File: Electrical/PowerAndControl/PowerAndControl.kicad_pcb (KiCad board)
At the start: 2 copper layers, 65 x 30 mm, 21 parts, among them J1 Conn_02x03_Counter_Clockwise, SW2 SW_SPDT_312, U1 MCP73811T-420I-OT, U2 TPS22919QDCKRQ1, U3 TPS3840PL30DBVR

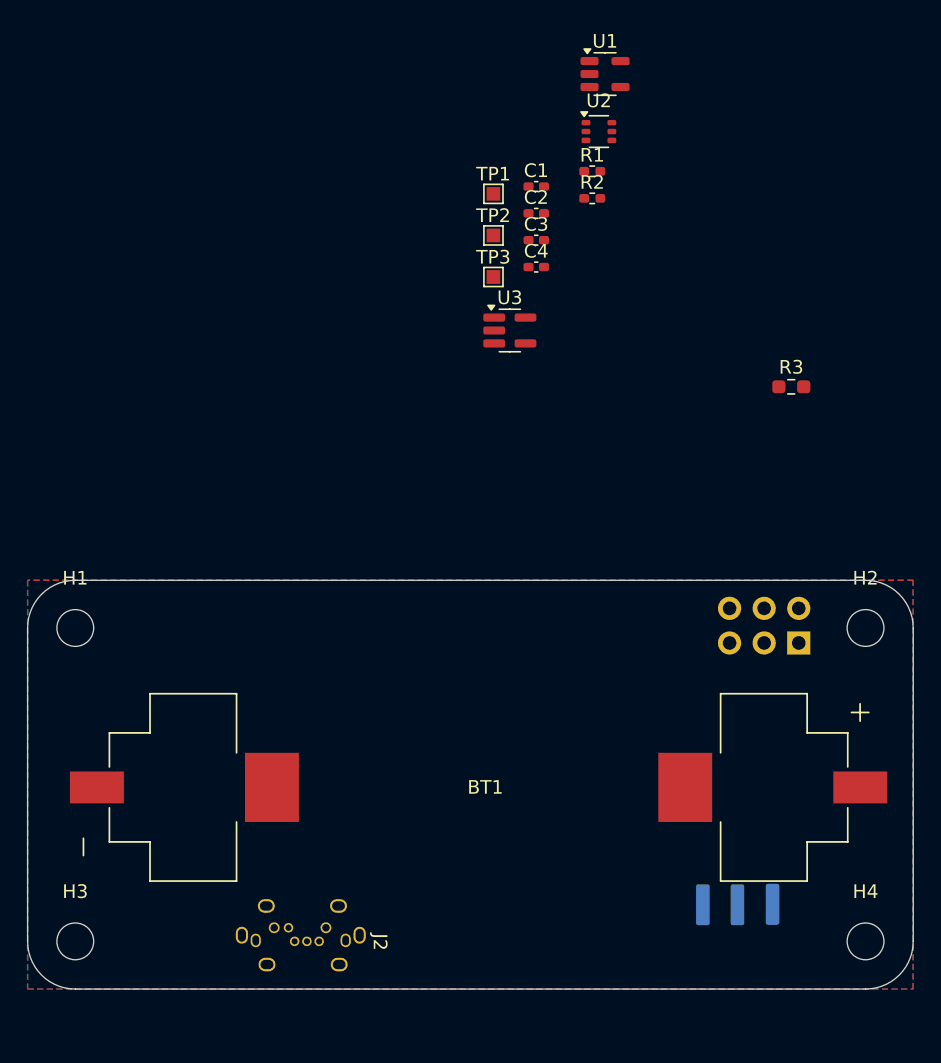
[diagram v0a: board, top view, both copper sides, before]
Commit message: Layout of AA variant complete.  Need to check pinout 2x more
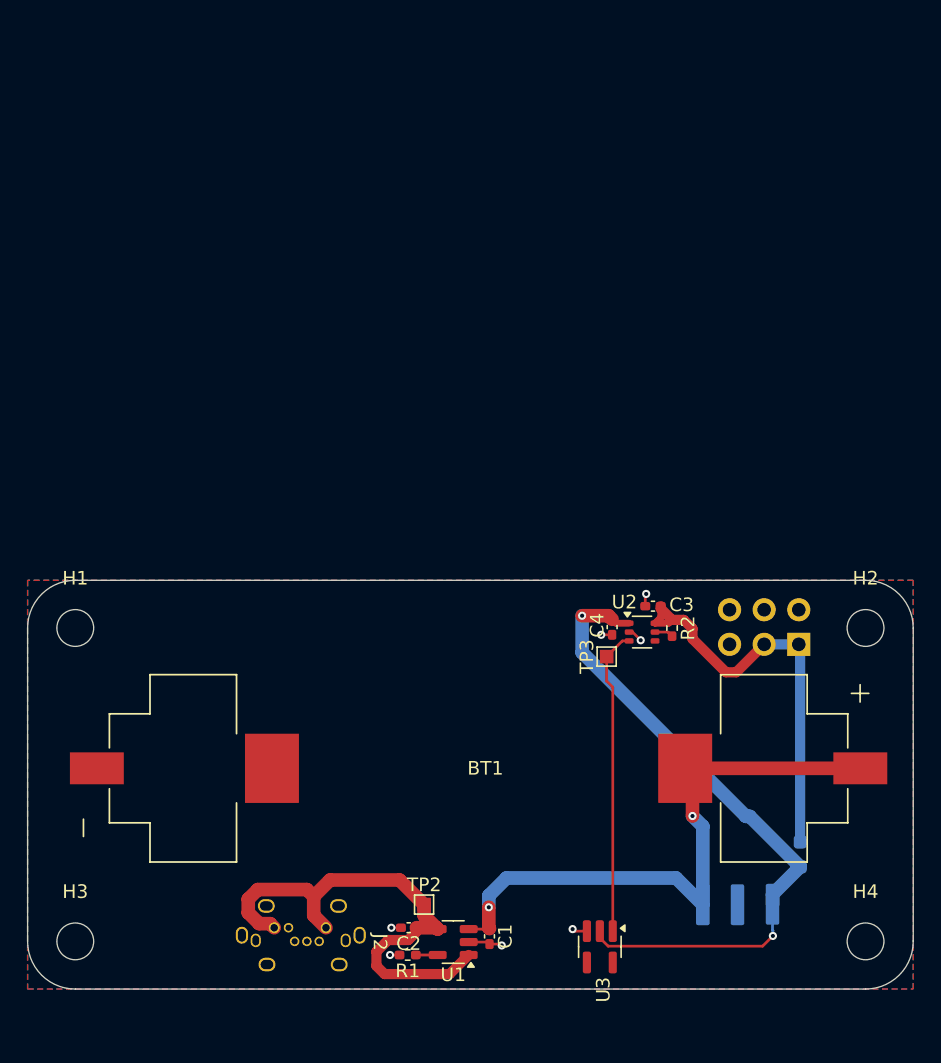
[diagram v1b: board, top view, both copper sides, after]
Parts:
- removed TP1: TestPoint, TestPoint:TestPoint_Pad_1.0x1.0mm
- R3: moved to B.Cu
- moved U1 64.7 mm to (127.7, 123.0), turned to 180 degrees
- moved R1 59.1 mm to (124.4, 124.0), turned to 180 degrees
- moved C1 55.1 mm to (130.4, 122.6), turned to -90 degrees
- moved C2 53.3 mm to (124.5, 122.0), turned to 180 degrees
- moved TP2 49.4 mm to (125.6, 120.3)
- moved U3 45.7 mm to (138.5, 123.4), turned to -90 degrees
- moved U2 36.9 mm to (141.6, 100.3)
- moved R3 34.3 mm to (153.2, 116.6), turned to 90 degrees
- moved R2 32.1 mm to (143.8, 100.0), turned to -90 degrees
- moved TP3 29.1 mm to (139.0, 102.1), turned to 90 degrees
- moved C3 28.2 mm to (142.4, 98.4), turned to 180 degrees
- moved C4 27.0 mm to (139.4, 99.9), turned to -90 degrees
- moved BT1 1.40 mm to (129.6, 110.3)
- moved J1 0.10 mm to (153.1, 101.2)
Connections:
- J1 pad 1: unconnected-(J1-Pin_1-Pad1) -> /VBAT_OUT
- J1 pad 3: unconnected-(J1-Pin_3-Pad3) -> /VBAT_OUT
- J1 pad 4: GND -> unconnected-(J1-Pin_4-Pad4)
- J1 pad 5: /VBAT_OUT -> GND
- J1 pad 6: /VBAT_OUT -> unconnected-(J1-Pin_6-Pad6)
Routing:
- net /VBAT: track 0.00 -> 48.6 mm, vias 0 -> 2
- net Net-(BT1-+): track 0.00 -> 44.4 mm, vias 0 -> 2
- net VBUS: track 0.00 -> 37.0 mm
- net /VBAT_OUT: track 0.00 -> 31.0 mm
- net /MONITOR: track 0.00 -> 22.5 mm
- net GND: track 0.00 -> 7.87 mm, vias 0 -> 7
- net Net-(U1-PROG): track 0.00 -> 1.61 mm
- net Net-(U2-QOD): track 0.00 -> 1.37 mm

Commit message: Cleaner Schematic / LED Indicators, better Layout
Added 3 LEDs for indicators.
Shcematic Cleaned up in general.
New Charger component
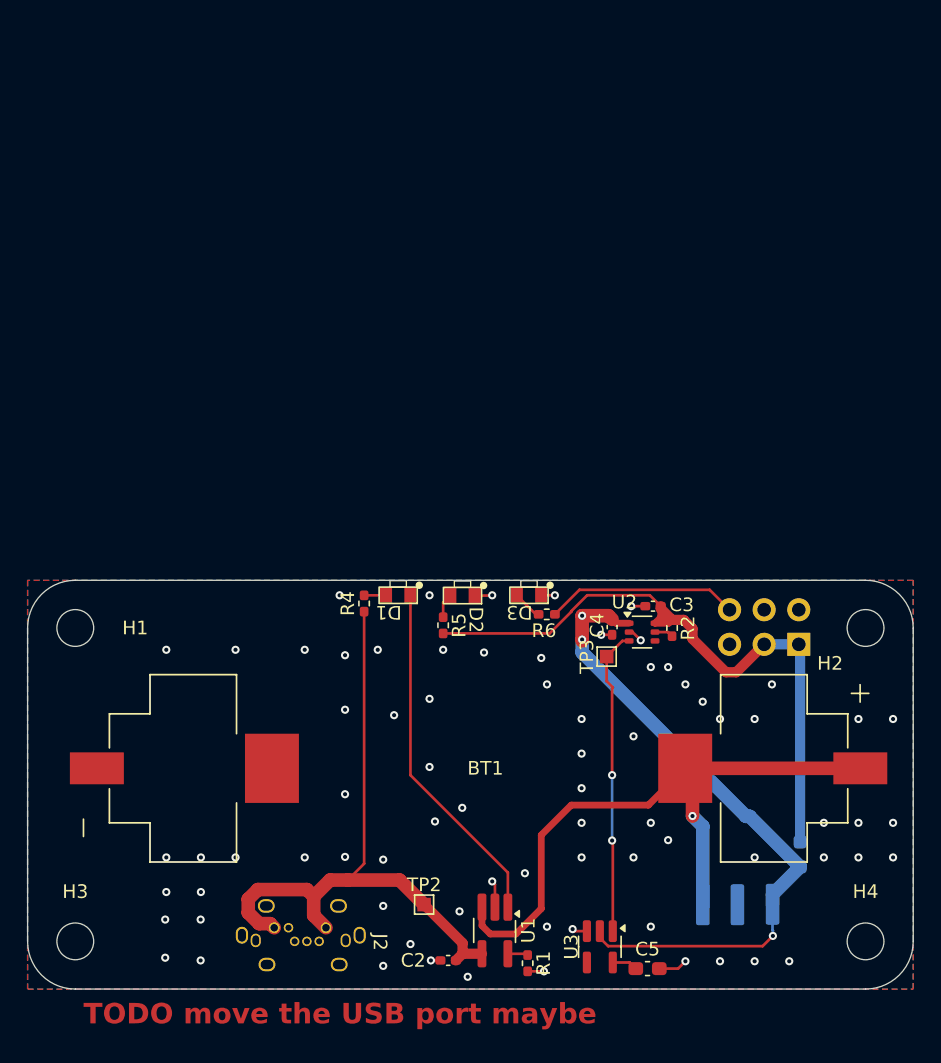
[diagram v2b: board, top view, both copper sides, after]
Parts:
- removed C1: 1u, Capacitor_SMD:C_0402_1005Metric_Pad0.74x0.62mm_HandSolder
- added C5: 1u, Capacitor_SMD:C_0603_1608Metric_Pad1.08x0.95mm_HandSolder, F.Cu at (142.0, 125.0)
- added D1: LED, Library:LED_0604, F.Cu at (124.6, 97.6)
- added D2: LED, Library:LED_0604, F.Cu at (129.3, 97.6)
- added D3: LED, Library:LED_0604, F.Cu at (134.2, 97.6)
- added R4: 6.2k, Resistor_SMD:R_0402_1005Metric_Pad0.72x0.64mm_HandSolder, F.Cu at (121.2, 98.2)
- added R5: 6.2k, Resistor_SMD:R_0402_1005Metric_Pad0.72x0.64mm_HandSolder, F.Cu at (127.0, 99.8)
- added R6: 6.2k, Resistor_SMD:R_0402_1005Metric_Pad0.72x0.64mm_HandSolder, F.Cu at (134.6, 99.0)
- R1: value 2k -> 6.2k
- R2: value 1k -> 0
- U1: value MCP73811T-420I-OT -> STC4054GR; footprint Package_TO_SOT_SMD:SOT-23-5 -> Package_TO_SOT_SMD:TSOT-23-5_HandSoldering
- moved R1 8.82 mm to (133.2, 124.6), turned to -90 degrees
- moved C2 3.76 mm to (127.4, 124.4)
- moved U1 3.18 mm to (130.8, 122.2), turned to -90 degrees
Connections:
- net Net-(BT1-+) renamed /VBAT_PRESWITCH
- J1 pad 6: unconnected-(J1-Pin_6-Pad6) -> /FRAME_GPIO
- U1 pad 1: VBUS -> Net-(D1-K)
- U3 pad 5: unconnected-(U3-CT-Pad5) -> /CT
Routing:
- net Net-(D1-K): track 0.00 -> 25.9 mm
- net /VBAT_OUT: track 31.0 -> 49.4 mm
- net /FRAME_GPIO: track 0.00 -> 14.4 mm
- net VBUS: track 37.0 -> 47.8 mm
- net GND: track 7.87 -> 12.3 mm, vias 7 -> 76
- net /VBAT_PRESWITCH: track 44.4 -> 48.1 mm, vias 2 -> 1
- net Net-(D3-A): track 0.00 -> 2.18 mm
- net /CT: track 0.00 -> 1.87 mm
- net /VBAT: track 48.6 -> 50.4 mm, vias 2 -> 3
- net Net-(D2-A): track 0.00 -> 1.80 mm
- net Net-(D1-A): track 0.00 -> 1.60 mm
- net /MONITOR: vias 0 -> 2
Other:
- board text added: "TODO move the USB port maybe"

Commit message: Cleared a TODO
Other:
- board text removed: "TODO move the USB port maybe"
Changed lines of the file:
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@@
 		(layer "Edge.Cuts")
-	)
-	(gr_text "TODO move the USB port maybe"
-		(at 100.6 129.2 0)
-		(layer "F.Cu")
-		(effects
-			(font
-				(size 1.5 1.5)
-				(thickness 0.3)
-				(bold yes)
-			)
-			(justify left bottom)
-		)
 	)
 	(segment

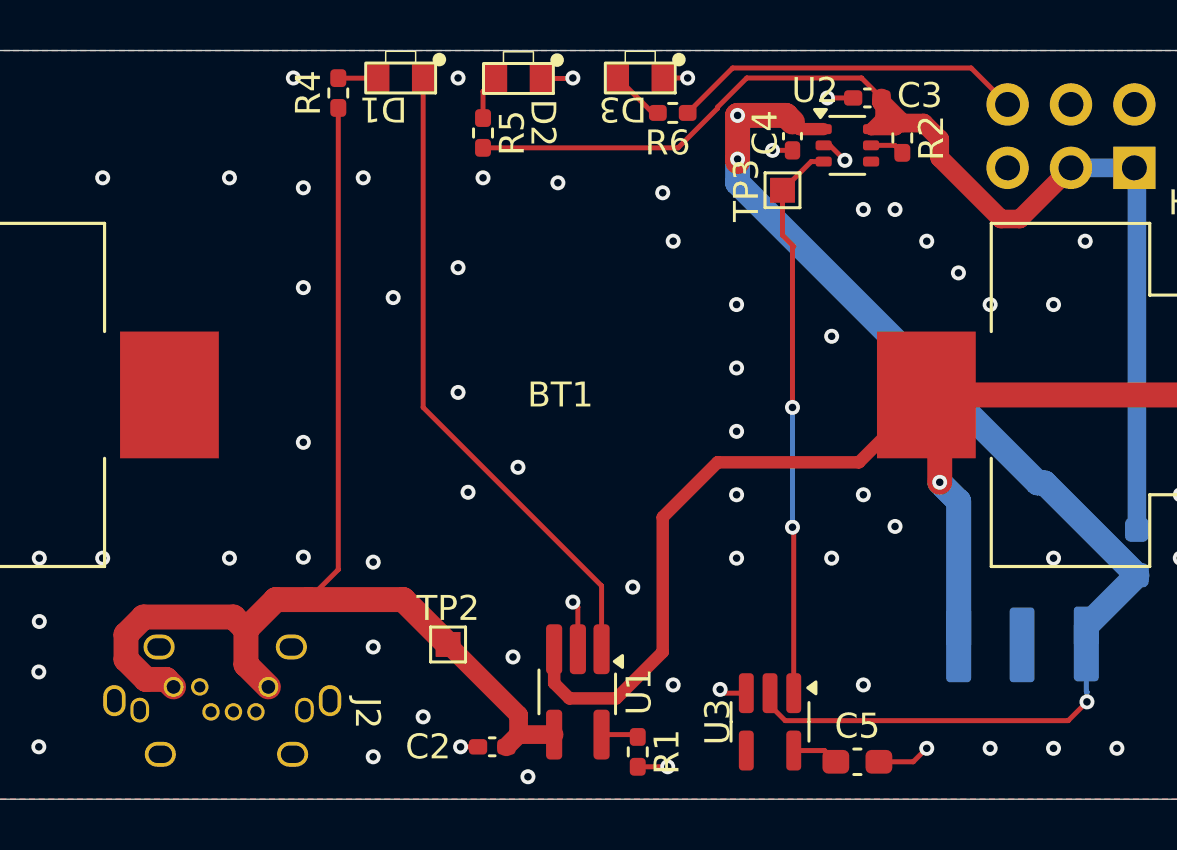
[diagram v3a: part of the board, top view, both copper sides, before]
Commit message: Added additional Silkscreen
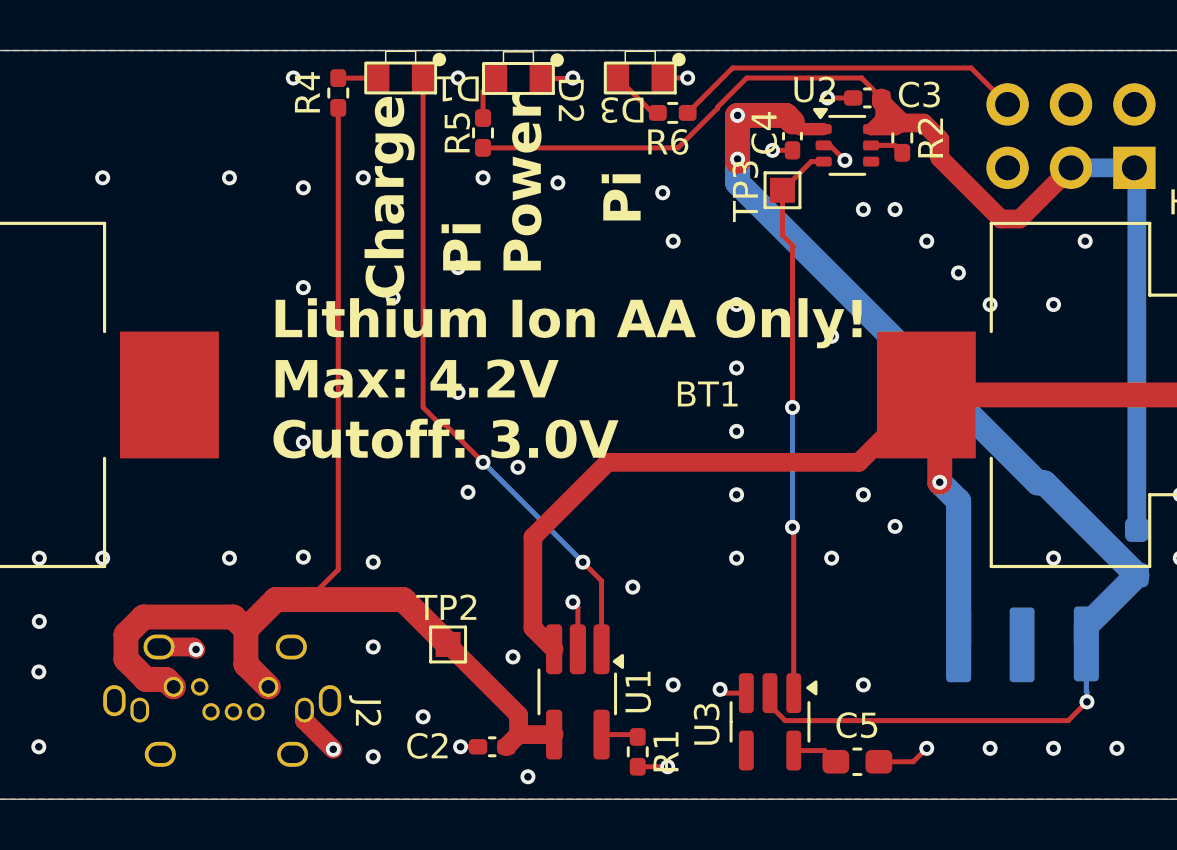
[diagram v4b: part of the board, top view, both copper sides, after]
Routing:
- net GND: track 12.3 -> 15.9 mm, vias 76 -> 78
- net /VBAT_PRESWITCH: track 48.1 -> 46.4 mm
- net Net-(D1-K): track 25.9 -> 26.0 mm, vias 0 -> 2
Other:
- board text added: "Charge"
- board text added: "Lithium Ion AA Only! Max: 4.2V Cutoff: 3.0V"
- board text added: "Pi"
- board text added: "Pi Power"
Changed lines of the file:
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@@
 		(tags "SC-74A TO_SOT_SMD")
 		(property "Reference" "U3"
-			(at 0 2.1 270)
+			(at 0.1 2.5 270)
 			(layer "F.SilkS")
 			(effects
@@
 		(at 129.318935 97.62 180)
 		(property "Reference" "D2"
-			(at -0.081065 -1.78 270)
+			(at -1.181065 -0.88 270)
 			(unlocked yes)
 			(layer "F.SilkS")
@@
 		)
 		(fp_text user "${REFERENCE}"
-			(at 1 1.95 180)
+			(at 0.818935 0.12 180)
 			(unlocked yes)
 			(layer "F.Fab")
@@
 		)
 		(fp_text user "${REFERENCE}"
-			(at 1 1.95 180)
+			(at 1 0.1 180)
 			(unlocked yes)
 			(layer "F.Fab")
@@
 		(tags "resistor handsolder")
 		(property "Reference" "R5"
-			(at 0 -1.17 90)
+			(at 0 1 90)
 			(layer "F.SilkS")
 			(effects
@@
 		(at 124.6 97.6 180)
 		(property "Reference" "D1"
-			(at 1.6 -1.25 180)
+			(at -1.4 -0.4 180)
 			(unlocked yes)
 			(layer "F.SilkS")
@@
 		)
 		(fp_text user "${REFERENCE}"
-			(at 1 1.95 180)
+			(at 1.1 0.1 180)
 			(unlocked yes)
 			(layer "F.Fab")
@@
 		(at 129.6 110.3 -90)
 		(property "Reference" "BT1"
-			(at 0 -0.499999 0)
+			(at 0 -6.4 0)
 			(layer "F.SilkS")
 			(effects
@@
 		(layer "Edge.Cuts")
 	)
-	(segment
-		(start 132.341 122.459)
-		(end 134.2 120.6)
-		(width 0.5)
-		(layer "F.Cu")
-		(net 1)
-	)
-	(segment
-		(start 130.459 122.459)
-		(end 132.341 122.459)
-		(width 0.5)
-		(layer "F.Cu")
-		(net 1)
+	(gr_text "Charge"
+		(at 124 106.5 90)
+		(layer "F.SilkS")
+		(effects
+			(font
+				(size 1.5 1.5)
+				(thickness 0.3)
+				(bold yes)
+			)
+			(justify left bottom)
+		)
+	)
+	(gr_text "Pi"
+		(at 133.5 103.5 90)
+		(layer "F.SilkS")
+		(effects
+			(font
+				(size 1.5 1.5)
+				(thickness 0.3)
+				(bold yes)
+			)
+			(justify left bottom)
+		)
+	)
+	(gr_text "Lithium Ion AA Only!\nMax: 4.2V\nCutoff: 3.0V"
+		(at 118.5 113 0)
+		(layer "F.SilkS")
+		(effects
+			(font
+				(size 1.5 1.5)
+				(thickness 0.3)
+				(bold yes)
+			)
+			(justify left bottom)
+		)
+	)
+	(gr_text "Pi\nPower"
+		(at 129.5 105.5 90)
+		(layer "F.SilkS")
+		(effects
+			(font
+				(size 1.5 1.5)
+				(thickness 0.3)
+				(bold yes)
+			)
+			(justify left bottom)
+		)
 	)
 	(segment
@@
 	)
 	(segment
-		(start 134.2 120.6)
-		(end 134.2 115.2)
-		(width 0.5)
+		(start 132 113)
+		(end 142.065 113)
+		(width 0.75)
 		(layer "F.Cu")
 		(net 1)
 	)
 	(segment
-		(start 129.85 120.49)
-		(end 129.85 121.85)
-		(width 0.5)
+		(start 129 119.64)
+		(end 129 116)
+		(width 0.75)
 		(layer "F.Cu")
 		(net 1)
 	)
 	(segment
-		(start 134.2 115.2)
-		(end 136.4 113)
-		(width 0.5)
+		(start 129.85 120.49)
+		(end 129 119.64)
+		(width 0.75)
 		(layer "F.Cu")
 		(net 1)
@@
 		(start 142.065 113)
 		(end 144.765 110.3)
-		(width 0.5)
-		(layer "F.Cu")
-		(net 1)
-	)
-	(segment
-		(start 129.85 121.85)
-		(end 130.459 122.459)
-		(width 0.5)
+		(width 0.75)
 		(layer "F.Cu")
 		(net 1)
@@
 	)
 	(segment
-		(start 136.4 113)
-		(end 142.065 113)
-		(width 0.5)
+		(start 129 116)
+		(end 132 113)
+		(width 0.75)
 		(layer "F.Cu")
 		(net 1)
@@
 	)
 	(segment
+		(start 114.02 120.4)
+		(end 115.4 120.4)
+		(width 0.75)
+		(layer "F.Cu")
+		(net 2)
+	)
+	(segment
 		(start 137.55 122.25)
 		(end 136.65 122.25)
@@
 	)
 	(segment
+		(start 119.845 123.345)
+		(end 121 124.5)
+		(width 0.75)
+		(layer "F.Cu")
+		(net 2)
+	)
+	(segment
+		(start 119.845 122.93)
+		(end 119.845 123.345)
+		(width 0.75)
+		(layer "F.Cu")
+		(net 2)
+	)
+	(segment
 		(start 140.65 100.3)
 		(end 140.9 100.3)
@@
 	)
 	(segment
+		(start 115.4 120.4)
+		(end 115.5 120.5)
+		(width 0.75)
+		(layer "F.Cu")
+		(net 2)
+	)
+	(segment
 		(start 139.4 100.5)
 		(end 138.6 100.5)
@@
 	)
 	(via
+		(at 121 124.5)
+		(size 0.6)
+		(drill 0.3)
+		(layers "F.Cu" "B.Cu")
+		(net 2)
+	)
+	(via
 		(at 106.68 116.84)
 		(size 0.6)
@@
 	)
 	(via
+		(at 115.5 120.5)
+		(size 0.6)
+		(drill 0.3)
+		(layers "F.Cu" "B.Cu")
+		(net 2)
+	)
+	(via
 		(at 142.24 102.87)
 		(size 0.6)
@@
 	(segment
 		(start 131.75 117.95)
-		(end 124.6 110.8)
+		(end 131.75 117.75)
 		(width 0.2)
 		(layer "F.Cu")
@@
 		(net 22)
 	)
+	(segment
+		(start 124.6 110.8)
+		(end 125.3 111.5)
+		(width 0.2)
+		(layer "F.Cu")
+		(net 22)
+	)
+	(segment
+		(start 131.75 117.75)
+		(end 131 117)
+		(width 0.2)
+		(layer "F.Cu")
+		(net 22)
+	)
+	(segment
+		(start 125.5 111.5)
+		(end 127 113)
+		(width 0.2)
+		(layer "F.Cu")
+		(net 22)
+	)
+	(segment
+		(start 125.3 111.5)
+		(end 125.5 111.5)
+		(width 0.2)
+		(layer "F.Cu")
+		(net 22)
+	)
+	(via
+		(at 127 113)
+		(size 0.6)
+		(drill 0.3)
+		(layers "F.Cu" "B.Cu")
+		(net 22)
+	)
+	(via
+		(at 131 117)
+		(size 0.6)
+		(drill 0.3)
+		(layers "F.Cu" "B.Cu")
+		(net 22)
+	)
+	(segment
+		(start 131 117)
+		(end 127 113)
+		(width 0.2)
+		(layer "B.Cu")
+		(net 22)
+	)
